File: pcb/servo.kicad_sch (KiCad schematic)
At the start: 1 part, among them J11 Conn_01x03_Pin

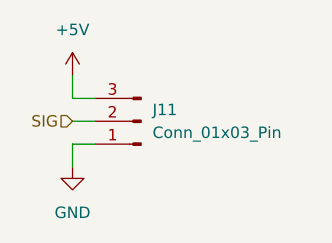
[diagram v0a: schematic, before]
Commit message: Remove sensor hub
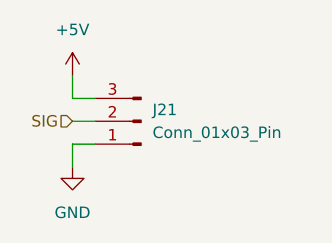
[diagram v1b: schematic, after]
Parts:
- J21: renamed from J11; footprint (none) -> Connector_PinHeader_2.54mm:PinHeader_1x03_P2.54mm_Vertical; LCSC (none) -> C6332196
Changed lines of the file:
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@@
 		(dnp no)
 		(fields_autoplaced yes)
-		(property "Reference" "#PWR0220"
+		(property "Reference" "#PWR0259"
 			(at 81.28 59.69 0)
 			(effects
@@
 			(project "raven"
 				(path "/38b0a34b-2047-47f6-90d7-ccdf77e8e212/7e3f67f4-c7a7-4f15-a62c-4903c0d88b19/48bd910e-1922-4cbf-82c0-63516f836aae"
-					(reference "#PWR0226")
+					(reference "#PWR0259")
 					(unit 1)
 				)
 				(path "/38b0a34b-2047-47f6-90d7-ccdf77e8e212/7e3f67f4-c7a7-4f15-a62c-4903c0d88b19/4b9f6c8c-5050-4109-94cd-845922bb9507"
-					(reference "#PWR0230")
+					(reference "#PWR0263")
 					(unit 1)
 				)
 				(path "/38b0a34b-2047-47f6-90d7-ccdf77e8e212/7e3f67f4-c7a7-4f15-a62c-4903c0d88b19/5f5322a5-6ca6-4329-b225-2e98f5af77fb"
-					(reference "#PWR0222")
+					(reference "#PWR0255")
 					(unit 1)
 				)
 				(path "/38b0a34b-2047-47f6-90d7-ccdf77e8e212/7e3f67f4-c7a7-4f15-a62c-4903c0d88b19/b34e6cdb-0429-4c8b-ab94-be7f1417c867"
-					(reference "#PWR0228")
+					(reference "#PWR0261")
 					(unit 1)
 				)
 				(path "/38b0a34b-2047-47f6-90d7-ccdf77e8e212/7e3f67f4-c7a7-4f15-a62c-4903c0d88b19/c43efd4d-e310-4bbf-b378-f4ca4f0e12c9"
-					(reference "#PWR0220")
+					(reference "#PWR0253")
 					(unit 1)
 				)
 				(path "/38b0a34b-2047-47f6-90d7-ccdf77e8e212/7e3f67f4-c7a7-4f15-a62c-4903c0d88b19/efc83594-e3fb-499b-a4ad-dd6a5dd5f24e"
-					(reference "#PWR0224")
+					(reference "#PWR0257")
 					(unit 1)
 				)
@@
 		(dnp no)
 		(fields_autoplaced yes)
-		(property "Reference" "#PWR0221"
+		(property "Reference" "#PWR0260"
 			(at 81.28 72.39 0)
 			(effects
@@
 			(project "raven"
 				(path "/38b0a34b-2047-47f6-90d7-ccdf77e8e212/7e3f67f4-c7a7-4f15-a62c-4903c0d88b19/48bd910e-1922-4cbf-82c0-63516f836aae"
-					(reference "#PWR0227")
+					(reference "#PWR0260")
 					(unit 1)
 				)
 				(path "/38b0a34b-2047-47f6-90d7-ccdf77e8e212/7e3f67f4-c7a7-4f15-a62c-4903c0d88b19/4b9f6c8c-5050-4109-94cd-845922bb9507"
-					(reference "#PWR0231")
+					(reference "#PWR0264")
 					(unit 1)
 				)
 				(path "/38b0a34b-2047-47f6-90d7-ccdf77e8e212/7e3f67f4-c7a7-4f15-a62c-4903c0d88b19/5f5322a5-6ca6-4329-b225-2e98f5af77fb"
-					(reference "#PWR0223")
+					(reference "#PWR0256")
 					(unit 1)
 				)
 				(path "/38b0a34b-2047-47f6-90d7-ccdf77e8e212/7e3f67f4-c7a7-4f15-a62c-4903c0d88b19/b34e6cdb-0429-4c8b-ab94-be7f1417c867"
-					(reference "#PWR0229")
+					(reference "#PWR0262")
 					(unit 1)
 				)
 				(path "/38b0a34b-2047-47f6-90d7-ccdf77e8e212/7e3f67f4-c7a7-4f15-a62c-4903c0d88b19/c43efd4d-e310-4bbf-b378-f4ca4f0e12c9"
-					(reference "#PWR0221")
+					(reference "#PWR0254")
 					(unit 1)
 				)
 				(path "/38b0a34b-2047-47f6-90d7-ccdf77e8e212/7e3f67f4-c7a7-4f15-a62c-4903c0d88b19/efc83594-e3fb-499b-a4ad-dd6a5dd5f24e"
-					(reference "#PWR0225")
+					(reference "#PWR0258")
 					(unit 1)
 				)
@@
 		(on_board yes)
 		(dnp no)
-		(property "Reference" "J11"
+		(property "Reference" "J21"
 			(at 90.17 59.6899 0)
 			(effects
@@
 			)
 		)
-		(property "Footprint" ""
+		(property "Footprint" "Connector_PinHeader_2.54mm:PinHeader_1x03_P2.54mm_Vertical"
 			(at 88.9 60.96 0)
 			(effects
@@
 		)
 		(property "Description" "Generic connector, single row, 01x03, script generated"
+			(at 88.9 60.96 0)
+			(effects
+				(font
+					(size 1.27 1.27)
+				)
+				(hide yes)
+			)
+		)
+		(property "LCSC" "C6332196"
 			(at 88.9 60.96 0)
 			(effects
@@
 			(project "raven"
 				(path "/38b0a34b-2047-47f6-90d7-ccdf77e8e212/7e3f67f4-c7a7-4f15-a62c-4903c0d88b19/48bd910e-1922-4cbf-82c0-63516f836aae"
-					(reference "J14")
+					(reference "J21")
 					(unit 1)
 				)
 				(path "/38b0a34b-2047-47f6-90d7-ccdf77e8e212/7e3f67f4-c7a7-4f15-a62c-4903c0d88b19/4b9f6c8c-5050-4109-94cd-845922bb9507"
-					(reference "J16")
+					(reference "J23")
 					(unit 1)
 				)
 				(path "/38b0a34b-2047-47f6-90d7-ccdf77e8e212/7e3f67f4-c7a7-4f15-a62c-4903c0d88b19/5f5322a5-6ca6-4329-b225-2e98f5af77fb"
-					(reference "J12")
+					(reference "J19")
 					(unit 1)
 				)
 				(path "/38b0a34b-2047-47f6-90d7-ccdf77e8e212/7e3f67f4-c7a7-4f15-a62c-4903c0d88b19/b34e6cdb-0429-4c8b-ab94-be7f1417c867"
-					(reference "J15")
+					(reference "J22")
 					(unit 1)
 				)
 				(path "/38b0a34b-2047-47f6-90d7-ccdf77e8e212/7e3f67f4-c7a7-4f15-a62c-4903c0d88b19/c43efd4d-e310-4bbf-b378-f4ca4f0e12c9"
-					(reference "J11")
+					(reference "J18")
 					(unit 1)
 				)
 				(path "/38b0a34b-2047-47f6-90d7-ccdf77e8e212/7e3f67f4-c7a7-4f15-a62c-4903c0d88b19/efc83594-e3fb-499b-a4ad-dd6a5dd5f24e"
-					(reference "J13")
-					(unit 1)
-				)
+					(reference "J20")
+					(unit 1)
+				)

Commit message: Finish schematic
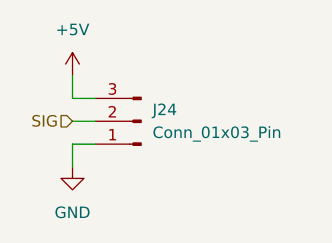
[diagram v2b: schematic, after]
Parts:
- renumbered J21 to J24
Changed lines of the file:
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@@
 		(dnp no)
 		(fields_autoplaced yes)
-		(property "Reference" "#PWR0259"
+		(property "Reference" "#PWR0257"
 			(at 81.28 59.69 0)
 			(effects
@@
 			(project "raven"
 				(path "/38b0a34b-2047-47f6-90d7-ccdf77e8e212/7e3f67f4-c7a7-4f15-a62c-4903c0d88b19/48bd910e-1922-4cbf-82c0-63516f836aae"
+					(reference "#PWR0257")
+					(unit 1)
+				)
+				(path "/38b0a34b-2047-47f6-90d7-ccdf77e8e212/7e3f67f4-c7a7-4f15-a62c-4903c0d88b19/4b9f6c8c-5050-4109-94cd-845922bb9507"
+					(reference "#PWR0261")
+					(unit 1)
+				)
+				(path "/38b0a34b-2047-47f6-90d7-ccdf77e8e212/7e3f67f4-c7a7-4f15-a62c-4903c0d88b19/5f5322a5-6ca6-4329-b225-2e98f5af77fb"
+					(reference "#PWR0253")
+					(unit 1)
+				)
+				(path "/38b0a34b-2047-47f6-90d7-ccdf77e8e212/7e3f67f4-c7a7-4f15-a62c-4903c0d88b19/b34e6cdb-0429-4c8b-ab94-be7f1417c867"
 					(reference "#PWR0259")
 					(unit 1)
 				)
-				(path "/38b0a34b-2047-47f6-90d7-ccdf77e8e212/7e3f67f4-c7a7-4f15-a62c-4903c0d88b19/4b9f6c8c-5050-4109-94cd-845922bb9507"
-					(reference "#PWR0263")
-					(unit 1)
-				)
-				(path "/38b0a34b-2047-47f6-90d7-ccdf77e8e212/7e3f67f4-c7a7-4f15-a62c-4903c0d88b19/5f5322a5-6ca6-4329-b225-2e98f5af77fb"
+				(path "/38b0a34b-2047-47f6-90d7-ccdf77e8e212/7e3f67f4-c7a7-4f15-a62c-4903c0d88b19/c43efd4d-e310-4bbf-b378-f4ca4f0e12c9"
+					(reference "#PWR0251")
+					(unit 1)
+				)
+				(path "/38b0a34b-2047-47f6-90d7-ccdf77e8e212/7e3f67f4-c7a7-4f15-a62c-4903c0d88b19/efc83594-e3fb-499b-a4ad-dd6a5dd5f24e"
 					(reference "#PWR0255")
-					(unit 1)
-				)
-				(path "/38b0a34b-2047-47f6-90d7-ccdf77e8e212/7e3f67f4-c7a7-4f15-a62c-4903c0d88b19/b34e6cdb-0429-4c8b-ab94-be7f1417c867"
-					(reference "#PWR0261")
-					(unit 1)
-				)
-				(path "/38b0a34b-2047-47f6-90d7-ccdf77e8e212/7e3f67f4-c7a7-4f15-a62c-4903c0d88b19/c43efd4d-e310-4bbf-b378-f4ca4f0e12c9"
-					(reference "#PWR0253")
-					(unit 1)
-				)
-				(path "/38b0a34b-2047-47f6-90d7-ccdf77e8e212/7e3f67f4-c7a7-4f15-a62c-4903c0d88b19/efc83594-e3fb-499b-a4ad-dd6a5dd5f24e"
-					(reference "#PWR0257")
 					(unit 1)
 				)
@@
 		(dnp no)
 		(fields_autoplaced yes)
-		(property "Reference" "#PWR0260"
+		(property "Reference" "#PWR0258"
 			(at 81.28 72.39 0)
 			(effects
@@
 			(project "raven"
 				(path "/38b0a34b-2047-47f6-90d7-ccdf77e8e212/7e3f67f4-c7a7-4f15-a62c-4903c0d88b19/48bd910e-1922-4cbf-82c0-63516f836aae"
+					(reference "#PWR0258")
+					(unit 1)
+				)
+				(path "/38b0a34b-2047-47f6-90d7-ccdf77e8e212/7e3f67f4-c7a7-4f15-a62c-4903c0d88b19/4b9f6c8c-5050-4109-94cd-845922bb9507"
+					(reference "#PWR0262")
+					(unit 1)
+				)
+				(path "/38b0a34b-2047-47f6-90d7-ccdf77e8e212/7e3f67f4-c7a7-4f15-a62c-4903c0d88b19/5f5322a5-6ca6-4329-b225-2e98f5af77fb"
+					(reference "#PWR0254")
+					(unit 1)
+				)
+				(path "/38b0a34b-2047-47f6-90d7-ccdf77e8e212/7e3f67f4-c7a7-4f15-a62c-4903c0d88b19/b34e6cdb-0429-4c8b-ab94-be7f1417c867"
 					(reference "#PWR0260")
 					(unit 1)
 				)
-				(path "/38b0a34b-2047-47f6-90d7-ccdf77e8e212/7e3f67f4-c7a7-4f15-a62c-4903c0d88b19/4b9f6c8c-5050-4109-94cd-845922bb9507"
-					(reference "#PWR0264")
-					(unit 1)
-				)
-				(path "/38b0a34b-2047-47f6-90d7-ccdf77e8e212/7e3f67f4-c7a7-4f15-a62c-4903c0d88b19/5f5322a5-6ca6-4329-b225-2e98f5af77fb"
+				(path "/38b0a34b-2047-47f6-90d7-ccdf77e8e212/7e3f67f4-c7a7-4f15-a62c-4903c0d88b19/c43efd4d-e310-4bbf-b378-f4ca4f0e12c9"
+					(reference "#PWR0252")
+					(unit 1)
+				)
+				(path "/38b0a34b-2047-47f6-90d7-ccdf77e8e212/7e3f67f4-c7a7-4f15-a62c-4903c0d88b19/efc83594-e3fb-499b-a4ad-dd6a5dd5f24e"
 					(reference "#PWR0256")
-					(unit 1)
-				)
-				(path "/38b0a34b-2047-47f6-90d7-ccdf77e8e212/7e3f67f4-c7a7-4f15-a62c-4903c0d88b19/b34e6cdb-0429-4c8b-ab94-be7f1417c867"
-					(reference "#PWR0262")
-					(unit 1)
-				)
-				(path "/38b0a34b-2047-47f6-90d7-ccdf77e8e212/7e3f67f4-c7a7-4f15-a62c-4903c0d88b19/c43efd4d-e310-4bbf-b378-f4ca4f0e12c9"
-					(reference "#PWR0254")
-					(unit 1)
-				)
-				(path "/38b0a34b-2047-47f6-90d7-ccdf77e8e212/7e3f67f4-c7a7-4f15-a62c-4903c0d88b19/efc83594-e3fb-499b-a4ad-dd6a5dd5f24e"
-					(reference "#PWR0258")
 					(unit 1)
 				)
@@
 		(on_board yes)
 		(dnp no)
-		(property "Reference" "J21"
+		(property "Reference" "J24"
 			(at 90.17 59.6899 0)
 			(effects
@@
 			(project "raven"
 				(path "/38b0a34b-2047-47f6-90d7-ccdf77e8e212/7e3f67f4-c7a7-4f15-a62c-4903c0d88b19/48bd910e-1922-4cbf-82c0-63516f836aae"
+					(reference "J24")
+					(unit 1)
+				)
+				(path "/38b0a34b-2047-47f6-90d7-ccdf77e8e212/7e3f67f4-c7a7-4f15-a62c-4903c0d88b19/4b9f6c8c-5050-4109-94cd-845922bb9507"
+					(reference "J26")
+					(unit 1)
+				)
+				(path "/38b0a34b-2047-47f6-90d7-ccdf77e8e212/7e3f67f4-c7a7-4f15-a62c-4903c0d88b19/5f5322a5-6ca6-4329-b225-2e98f5af77fb"
+					(reference "J22")
+					(unit 1)
+				)
+				(path "/38b0a34b-2047-47f6-90d7-ccdf77e8e212/7e3f67f4-c7a7-4f15-a62c-4903c0d88b19/b34e6cdb-0429-4c8b-ab94-be7f1417c867"
+					(reference "J25")
+					(unit 1)
+				)
+				(path "/38b0a34b-2047-47f6-90d7-ccdf77e8e212/7e3f67f4-c7a7-4f15-a62c-4903c0d88b19/c43efd4d-e310-4bbf-b378-f4ca4f0e12c9"
 					(reference "J21")
 					(unit 1)
 				)
-				(path "/38b0a34b-2047-47f6-90d7-ccdf77e8e212/7e3f67f4-c7a7-4f15-a62c-4903c0d88b19/4b9f6c8c-5050-4109-94cd-845922bb9507"
+				(path "/38b0a34b-2047-47f6-90d7-ccdf77e8e212/7e3f67f4-c7a7-4f15-a62c-4903c0d88b19/efc83594-e3fb-499b-a4ad-dd6a5dd5f24e"
 					(reference "J23")
 					(unit 1)
 				)
-				(path "/38b0a34b-2047-47f6-90d7-ccdf77e8e212/7e3f67f4-c7a7-4f15-a62c-4903c0d88b19/5f5322a5-6ca6-4329-b225-2e98f5af77fb"
-					(reference "J19")
-					(unit 1)
-				)
-				(path "/38b0a34b-2047-47f6-90d7-ccdf77e8e212/7e3f67f4-c7a7-4f15-a62c-4903c0d88b19/b34e6cdb-0429-4c8b-ab94-be7f1417c867"
-					(reference "J22")
-					(unit 1)
-				)
-				(path "/38b0a34b-2047-47f6-90d7-ccdf77e8e212/7e3f67f4-c7a7-4f15-a62c-4903c0d88b19/c43efd4d-e310-4bbf-b378-f4ca4f0e12c9"
-					(reference "J18")
-					(unit 1)
-				)
-				(path "/38b0a34b-2047-47f6-90d7-ccdf77e8e212/7e3f67f4-c7a7-4f15-a62c-4903c0d88b19/efc83594-e3fb-499b-a4ad-dd6a5dd5f24e"
-					(reference "J20")
-					(unit 1)
-				)

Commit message: Add power switch
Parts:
- J24: now not fitted
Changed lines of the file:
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@@
 		(in_bom yes)
 		(on_board yes)
-		(dnp no)
+		(dnp yes)
 		(property "Reference" "J24"
 			(at 90.17 59.6899 0)

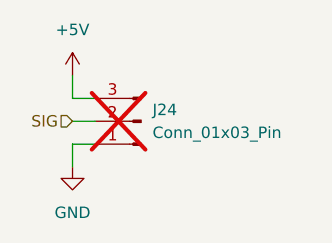
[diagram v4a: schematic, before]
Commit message: Finish schematic
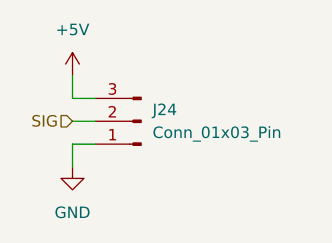
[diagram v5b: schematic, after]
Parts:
- J24: now fitted
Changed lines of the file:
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@@
 		(in_bom yes)
 		(on_board yes)
-		(dnp yes)
+		(dnp no)
 		(property "Reference" "J24"
 			(at 90.17 59.6899 0)
